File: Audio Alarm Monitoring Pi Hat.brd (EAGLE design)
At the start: 23.8 x 56 mm, 7 parts, among them J1 35RAPC4BHN2, J2 2X6 FEMALE

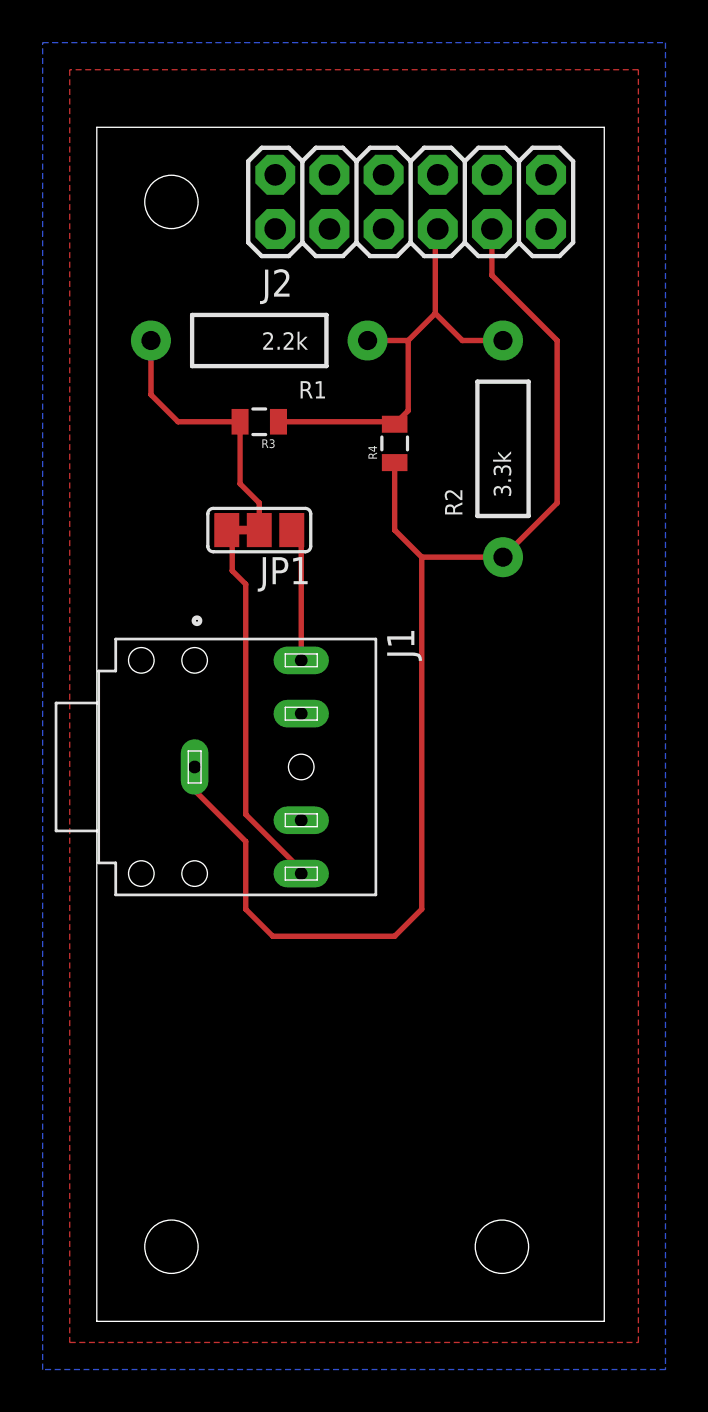
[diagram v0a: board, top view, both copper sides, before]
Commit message: Updating for LED + all surface mount resistors
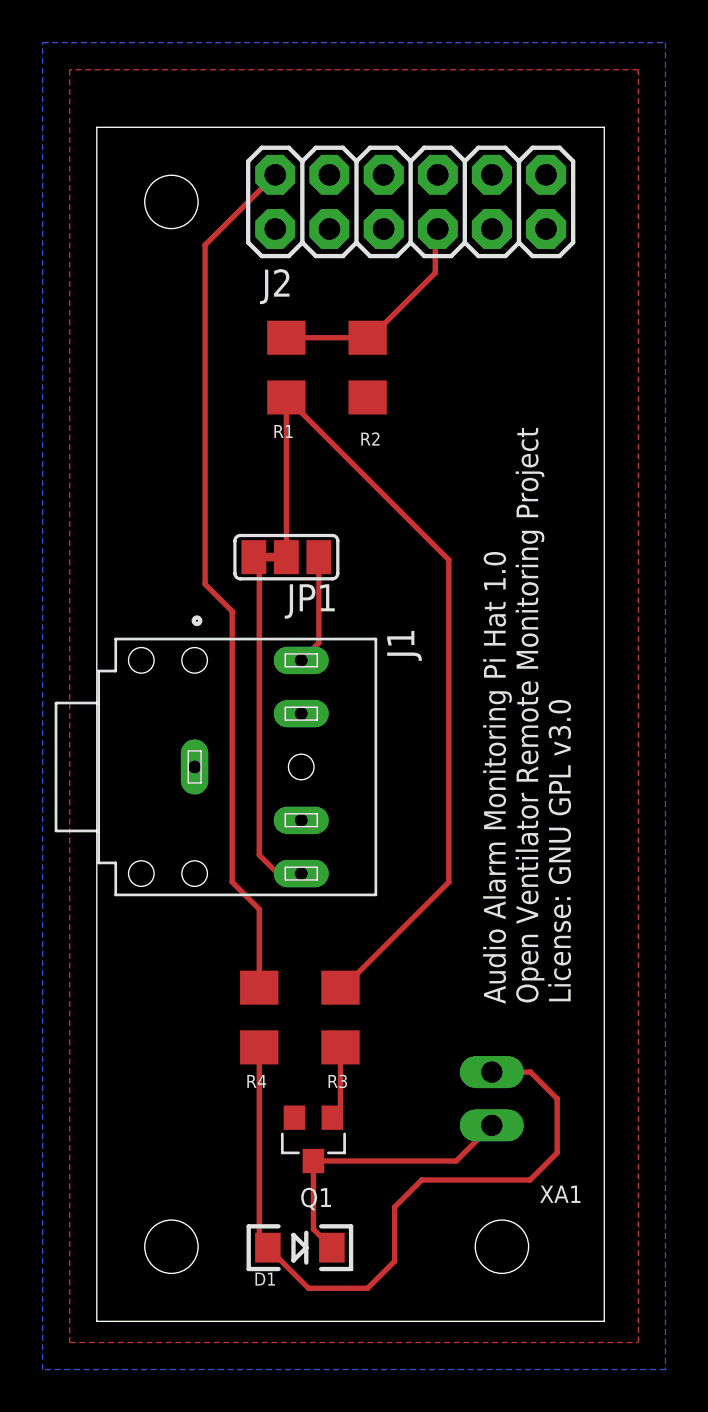
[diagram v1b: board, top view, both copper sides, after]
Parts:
- added D1: (no value), SparkFun-LED:LED-1206
- added Q1: SMD-TRANSISTORS-NPN-25V-500MW(SOT-23), SMD-TRANSISTORS-NPN-25V-500MW_SOT-23_:SOT-23
- added XA1: XHP-2, XHP-2:JST_XHP-2
- R1, R2: device SparkFun-Resistors:AXIAL-0.4 -> SparkFun-Passives:1206
- R3: value 2.2k -> 4.7k; device SparkFun-Passives:0805 -> SparkFun-Passives:1206
- R4: value 3.3k -> 150; device SparkFun-Passives:0805 -> SparkFun-Passives:1206
- moved R3 28.2 mm to (11.4, 31.8), turned to 270 degrees
- moved R4 27.7 mm to (7.62, 31.8)
- moved R2 7.41 mm to (12.7, 62.2)
- moved R1 1.80 mm to (8.89, 62.2), turned to 270 degrees
- moved JP1 1.80 mm to (8.89, 53.3)
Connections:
- new net 5V: J2.2, R4.2
- new net N$5: D1.C, Q1.3, XA1.2
- new net N$8: D1.A, R4.1, XA1.1
- new net N$9: Q1.1, R3.2
- net GND: now also Q1.2, R2.1; no longer R2.P$1, R4.1
- net N$1: now also R1.1, R2.2; no longer R1.P$1, R2.P$2, R3.1, R4.2
- net N$2: now also R1.2, R3.1; no longer R1.P$2, R3.2
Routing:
- net GND: track 60.0 -> 0.00 mm
- net 5V: track 0.00 -> 40.5 mm
- net N$8: track 0.00 -> 34.2 mm
- net N$2: track 12.7 -> 40.5 mm
- net N$5: track 0.00 -> 13.5 mm
- net N$1: track 21.1 -> 10.3 mm
- net N$9: track 0.00 -> 4.22 mm
- net N$4: track 17.6 -> 16.4 mm
- net N$6: track 6.29 -> 5.18 mm
- added copper zone on layer 1, net GND
- added copper zone on layer 16, net GND
- removed copper zone on layer 1, net N$3
- removed copper zone on layer 16, net N$7
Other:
- board text added: "Audio Alarm Monitoring Pi Hat 1.0 Open Ventilator Remote Monitoring Project License: GNU GPL v3.0"
- board text added: "SS8050"
- board text removed: "Audio Alarm Monitoring Pi Hat 1.0"
